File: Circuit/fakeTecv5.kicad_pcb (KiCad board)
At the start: 2 copper layers, 25.4 x 52.1 mm, 76 parts, among them J1 EXTRA, J11 FET1 3,3, J12 FET2 3,3, J13 FET3 3,3, J14 GPS Pins, J16 Encoder Pads, J37 SCL, J38 JST-SH-4, J39 SDA, J40 3.3V, J41 GND, J42 FET1, J43 FET2, J44 FET3, J45 GND, J46 Conn_01x02_Socket, J47 GND, J48 GND, J49 GND, J5 I2C Oled screen, J50 JST-SH-4, J6 FET1 Drain, J7 FET2 Drain, J8 FET3 Drain, J9 Molex PicoBlade 0532610271, Q1 AO3400A, Q2 AO3400A, Q3 AO3400A, SW1 Reset, SW2 SW_Push, U1 XB8089D0, U2 HT-RA62, U3 nice!nano v2

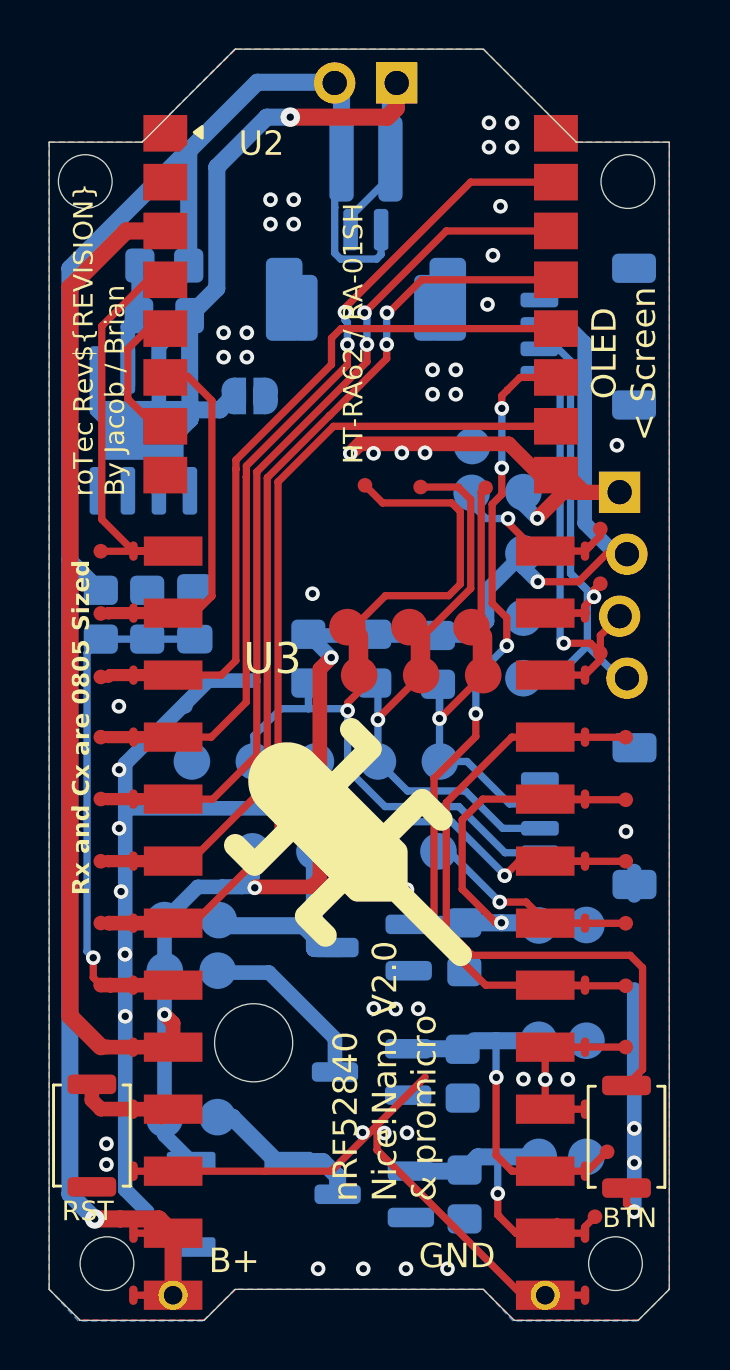
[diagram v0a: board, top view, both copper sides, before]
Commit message: hw: Add GPS slot and mark as Rev5.2
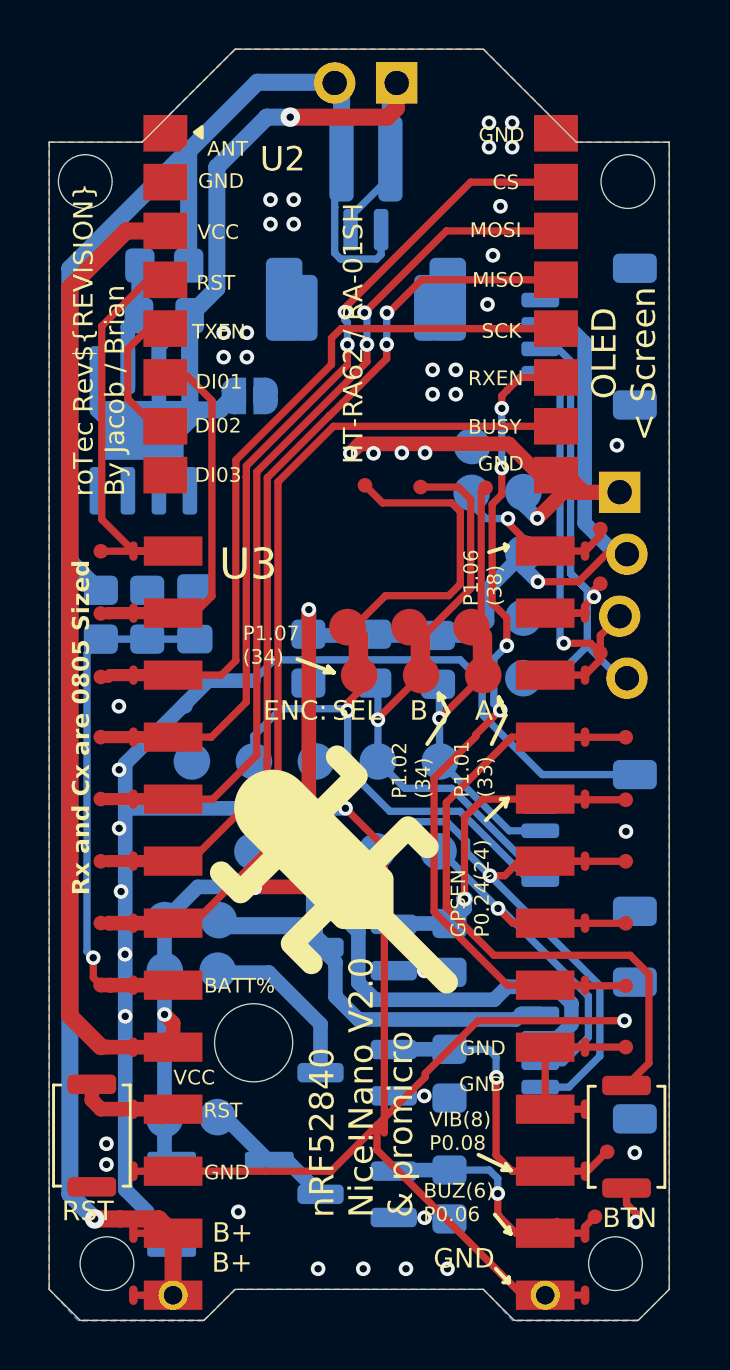
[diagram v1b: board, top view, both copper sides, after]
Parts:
- removed J42: FET1, faketec:SMD_PAD_1x01
- removed J43: FET2, faketec:SMD_PAD_1x01
- removed J44: FET3, faketec:SMD_PAD_1x01
- removed J47, J48, J49: GND, faketec:SMD_PAD_1x01
- added J51: JST-SH-4, Connector_JST:JST_SH_SM04B-SRSS-TB_1x04-1MP_P1.00mm_Horizontal, B.Cu at (121.0, 68.0)
- moved J50 1.10 mm to (121.0, 59.5)
- moved BZ1 0.80 mm to (105.9, 74.3)
- moved Q3 0.70 mm to (111.5, 73.9)
- moved R3 0.62 mm to (115.3, 73.9)
- moved R1 0.61 mm to (115.3, 63.8)
- moved Q1 0.61 mm to (111.5, 63.8)
- moved Q2 0.59 mm to (111.5, 68.9)
- moved R2 0.54 mm to (115.3, 69.0)
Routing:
- net GND: track 93.8 -> 126.1 mm, vias 55 -> 46
- net +3.3V: track 100.8 -> 119.5 mm, vias 4 -> 5
- net /GPSRX: track 12.0 -> 24.5 mm
- net /GPS_GND: track 10.6 -> 20.0 mm
- net /GPSTX: track 8.94 -> 18.2 mm
- net /FET1: track 17.5 -> 13.8 mm
- net /FET3: track 12.2 -> 9.71 mm
- net /FET2: track 12.5 -> 11.2 mm
- net /BUZZER: track 6.72 -> 5.53 mm
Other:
- board text added: "10KΩ: R1,R2,R3"
- board text added: "<5020 Buzzer"
- board text added: "<GPS Module"
- board text added: "A&O AO3400A nchn mosfet: Q1, Q2, Q3"
- board text added: "ANT"
- board text added: "BATT%"
- board text added: "BUSY"
- board text added: "BUZ(6) P0.06"
- board text added: "CS"
- board text added: "D"
- board text added: "DI01"
- board text added: "DI02"
- board text added: "DI03"
- board text added: "ENC:"
- board text added: "ENCODER"
- board text added: "G"
- board text added: "GPS"
- board text added: "GPSEN P0.24(24)"
- board text added: "MISO"
- board text added: "MOSI"
- board text added: "P1.01 (33)"
- board text added: "P1.02 (34)"
- board text added: "P1.06 (38)"
- board text added: "P1.07 (34)"
- board text added: "RXEN"
- board text added: "S"
- board text added: "SCK"
- board text added: "TXEN"
- board text added: "VIB(8) P0.08"
- board text removed: "5020 Buzzer >"
- board text removed: "<GPS"
- board text removed: "ENC"
- board text removed: "P0.06( 6)"
- board text removed: "P0.08( 8)"
- board text removed: "P0.24(24)"
- board text removed: "Push"

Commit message: hw: silkscreen correction to ENC_PUSH. Marked as Rev5.2.1
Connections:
- Q1 pad 1: /FET1 -> /FET1_GPSEN
- Q2 pad 1: /FET2 -> /FET2_VIB
- Q3 pad 1: /FET3 -> /FET3_BUZ
- R1 pad 2: /FET1 -> /FET1_GPSEN
- R2 pad 2: /FET2 -> /FET2_VIB
- R3 pad 2: /FET3 -> /FET3_BUZ
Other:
- board text added: "P1.07 (39)"
- board text removed: "P1.07 (34)"
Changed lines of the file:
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@@
 		)
 	)
-	(property "REVISION" "5.2")
+	(property "REVISION" "5.2.1")
 	(net 0 "")
 	(net 1 "/Batt%")
@@
 	(net 32 "/ENC_PUSH")
 	(net 33 "/EXTRA")
+	(net 34 "/FET1_GPSEN")
+	(net 35 "/FET2_VIB")
+	(net 36 "/FET3_BUZ")
 	(footprint "MountingHole:MountingHole_3.2mm_M3"
 		(layer "F.Cu")
@@
 			(layers "B.Cu" "B.Mask" "B.Paste")
 			(roundrect_rratio 0.208333)
-			(net 21 "/FET3")
+			(net 36 "/FET3_BUZ")
 			(pintype "passive")
 		)
@@
 			(layers "B.Cu" "B.Mask" "B.Paste")
 			(roundrect_rratio 0.208333)
-			(net 19 "/FET2")
+			(net 35 "/FET2_VIB")
 			(pintype "passive")
 		)
@@
 			(layers "B.Cu" "B.Mask" "B.Paste")
 			(roundrect_rratio 0.25)
-			(net 17 "/FET1")
+			(net 34 "/FET1_GPSEN")
 			(pinfunction "G")
 			(pintype "input")
@@
 			(layers "B.Cu" "B.Mask" "B.Paste")
 			(roundrect_rratio 0.25)
-			(net 19 "/FET2")
+			(net 35 "/FET2_VIB")
 			(pinfunction "G")
 			(pintype "input")
@@
 			(layers "B.Cu" "B.Mask" "B.Paste")
 			(roundrect_rratio 0.208333)
-			(net 17 "/FET1")
+			(net 34 "/FET1_GPSEN")
 			(pintype "passive")
 		)
@@
 			(layers "B.Cu" "B.Mask" "B.Paste")
 			(roundrect_rratio 0.25)
-			(net 21 "/FET3")
+			(net 36 "/FET3_BUZ")
 			(pinfunction "G")
 			(pintype "input")
@@
 		)
 	)
-	(gr_text "P1.07\n(34)"
+	(gr_text "P1.07\n(39)"
 		(at 106.81 51.4 0)
 		(layer "F.SilkS")

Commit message: hw: optimise ground plane and add silkscreen to battery header. Mark as Rev5.2.2
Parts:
- moved J9 0.26 mm to (111.6, 34.3)
- moved J46 0.22 mm to (112.9, 28.4)
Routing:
- net GND: track 126.1 -> 136.6 mm, vias 46 -> 55
- net /EXTRA: track 5.24 -> 6.40 mm
- net +BATT: track 76.8 -> 76.3 mm
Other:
- board text added: "BAT"

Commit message: hw: Fix silkscreen 680KΩ (Previously 680Ω)
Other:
- board text added: "680KΩ"
- board text removed: "680Ω"
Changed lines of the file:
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@@
 		)
 	)
-	(gr_text "680Ω"
+	(gr_text "680KΩ"
 		(at 100.11 48.53 90)
 		(layer "B.SilkS")

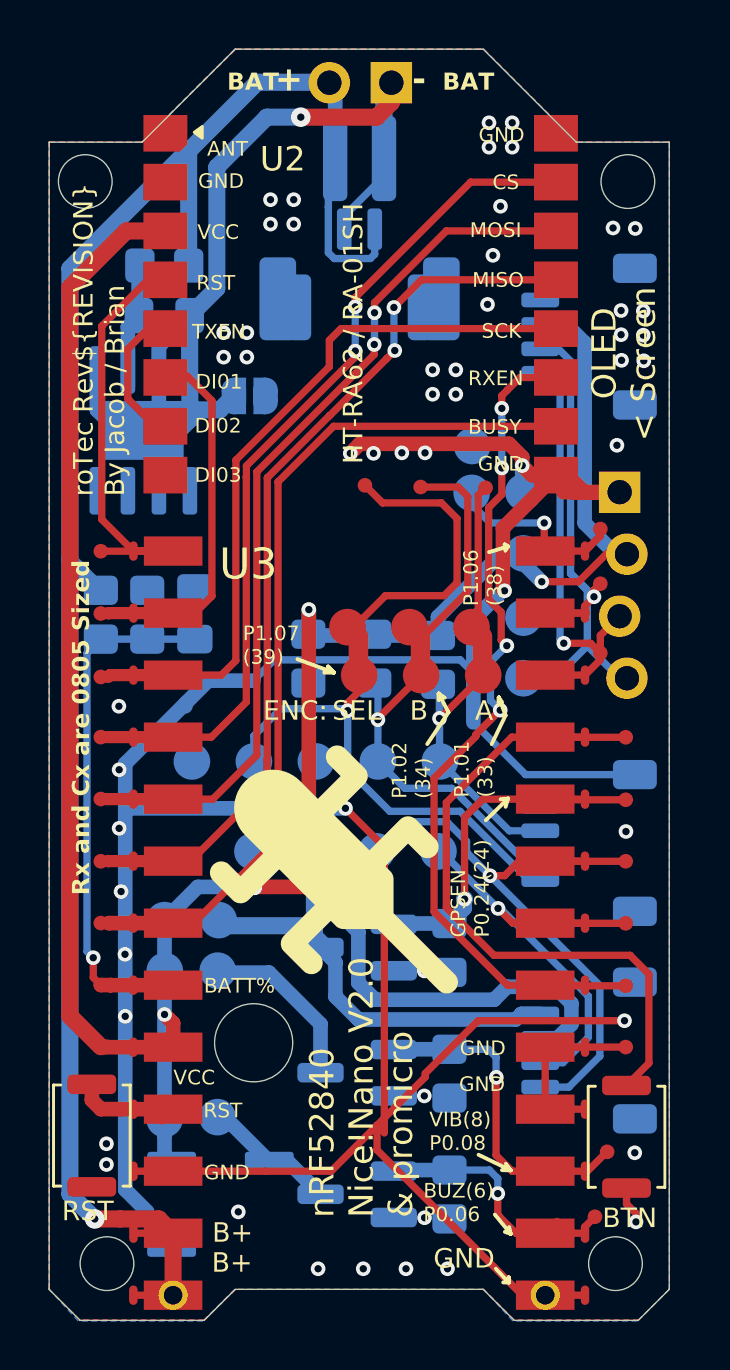
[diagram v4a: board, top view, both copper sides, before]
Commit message: hw: change footprint to rely on testpads on the nice!nano footprint instead
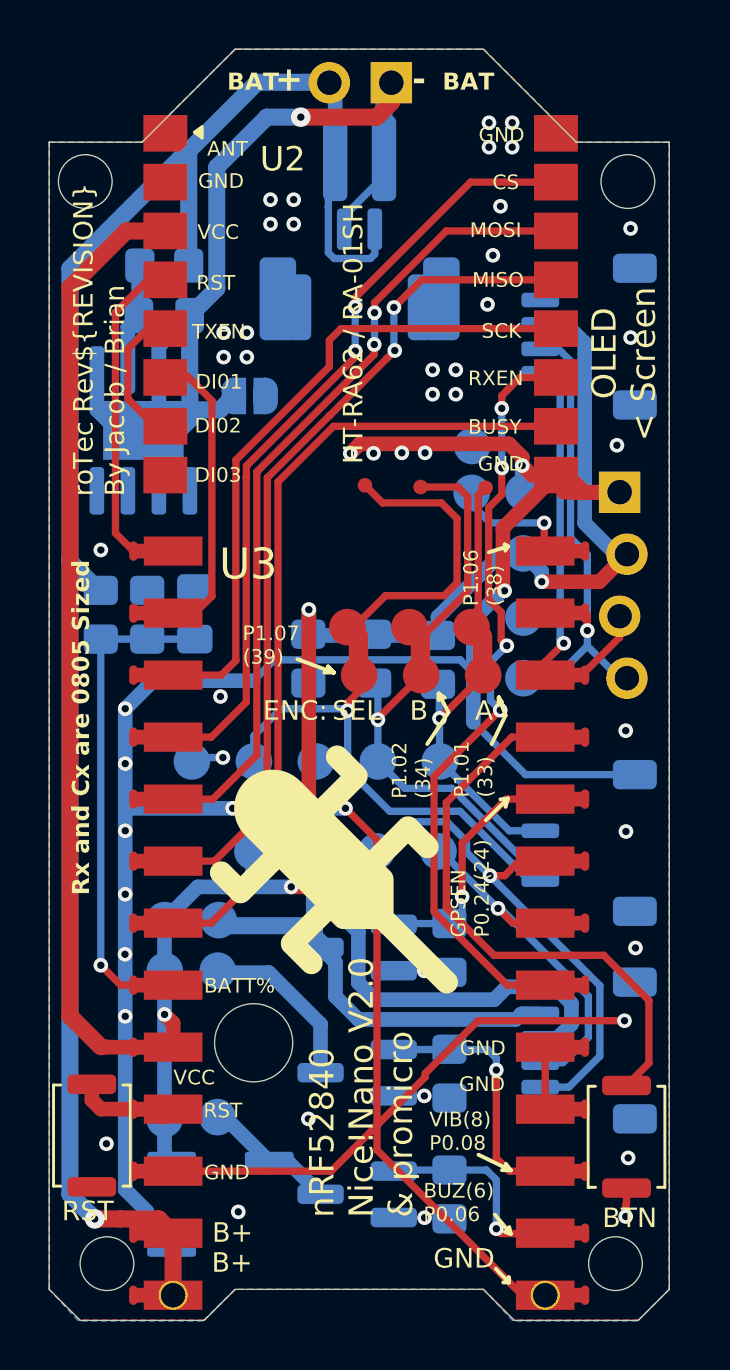
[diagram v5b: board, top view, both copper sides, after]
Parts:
- removed J10, J15, J17, J18, J19, J20, J21, J23, J24, J25, J26, J27, J28, J29, J30, J31, J32, J33, J34, J35, J36, J4: ~, faketec:TestPoint_Pad_Slim_D0.6mm
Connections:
- U3 pad 1: /FET3 -> /FET3_BUZ
- U3 pad 2: /FET2 -> /FET2_VIB
- U3 pad 8: /FET1 -> /FET1_GPSEN
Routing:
- net /FET1: track 13.8 -> 0.00 mm, vias 1 -> 0
- net /FET2: track 11.2 -> 0.00 mm, vias 1 -> 0
- net /FET2_VIB: track 0.00 -> 10.7 mm, vias 0 -> 1
- net /FET1_GPSEN: track 0.00 -> 9.95 mm, vias 0 -> 1
- net /FET3: track 9.71 -> 0.00 mm, vias 1 -> 0
- net /FET3_BUZ: track 0.00 -> 9.52 mm, vias 0 -> 1
- net /BTN: track 27.2 -> 23.3 mm
- net /SDA: track 24.1 -> 20.4 mm
- net /RST: track 17.7 -> 14.3 mm
- net /GPSTX: track 18.2 -> 14.9 mm
- net /GPSRX: track 24.5 -> 21.2 mm
- net /RXEN: track 35.0 -> 31.7 mm
- net /CS: track 35.0 -> 32.2 mm
- net /MOSI: track 36.1 -> 33.3 mm
- net /SCK: track 29.9 -> 27.2 mm
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
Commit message: hw: Add makefile. Refine. Rev5.3
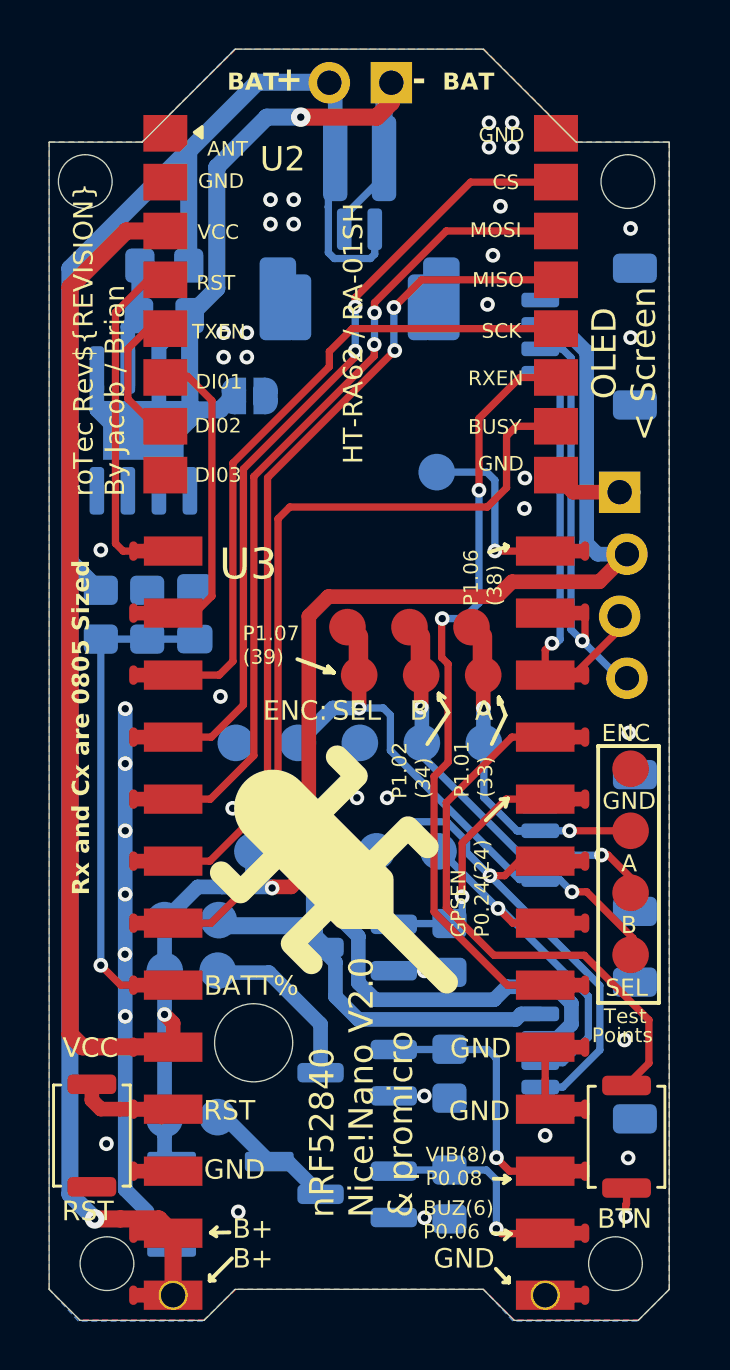
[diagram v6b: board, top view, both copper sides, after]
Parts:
- removed J22, J3: ~, faketec:TestPoint_Pad_Slim_D0.6mm
- removed J37: SCL, faketec:SMD_PAD_1x01
- removed J39: SDA, faketec:SMD_PAD_1x01
- removed J40: 3.3V, faketec:SMD_PAD_1x01
- removed J41, J45: GND, faketec:SMD_PAD_1x01
- removed R10, R11, R9: 10k, Resistor_SMD:R_0805_2012Metric_Pad1.20x1.40mm_HandSolder
- J2: value ~ -> Conn_01x04_Socket; footprint faketec:TestPoint_Pad_Slim_D0.6mm -> faketec:SMD_PAD_1x04
- moved J2 21.0 mm to (122.7, 64.1), turned to 90 degrees
- moved J16 1.95 mm to (106.5, 55.4)
- moved J1 1.66 mm to (114.8, 44.3)
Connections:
- J2 pad 1: /ENC_B -> /ENC_PUSH
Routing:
- net GND: track 135.4 -> 28.6 mm, vias 51 -> 40
- net /ENC_PUSH: track 33.2 -> 21.1 mm, vias 1 -> 2
- net /ENC_B: track 23.2 -> 14.1 mm, vias 1 -> 2
- net /ENC_A: track 18.7 -> 12.7 mm, vias 1 -> 2
- net /SDA: track 20.4 -> 17.7 mm
- net /EXTRA: track 4.93 -> 7.54 mm
- net +3.3V: track 119.8 -> 121.9 mm, vias 5 -> 2
- net /SCL: track 19.4 -> 17.6 mm
- net /RXEN: track 31.7 -> 31.5 mm, vias 4 -> 2
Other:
- board text added: "ENC"
- board text added: "Points"
- board text added: "Test"
- board text removed: "10KΩ"
